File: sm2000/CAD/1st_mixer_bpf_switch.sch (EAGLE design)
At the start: 45 parts, among them U1 ADE-1, U2 PGA-103+

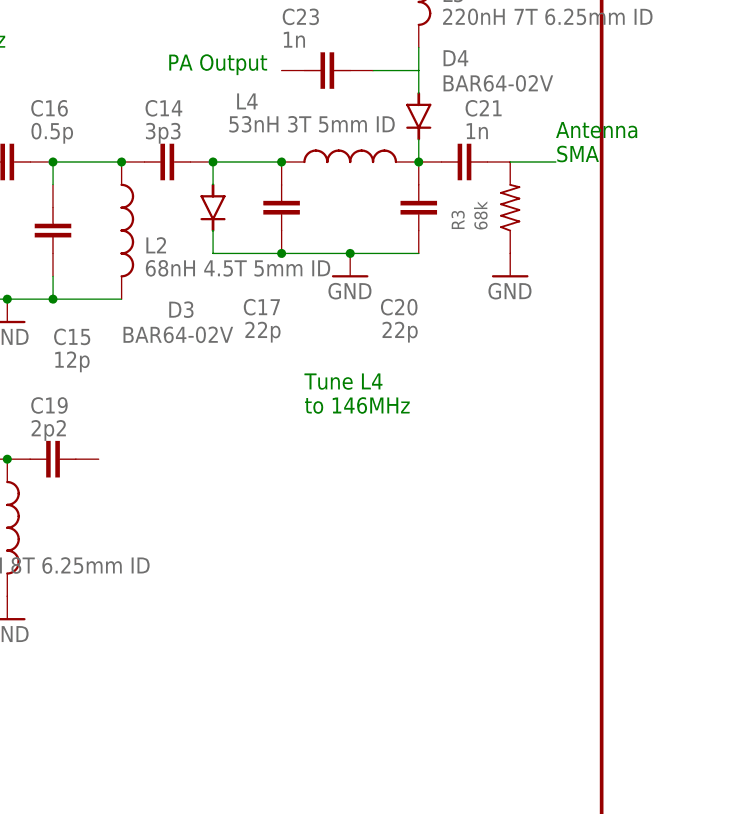
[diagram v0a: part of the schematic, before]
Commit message: added diode switch to TX 2nd lo and pwr sensor
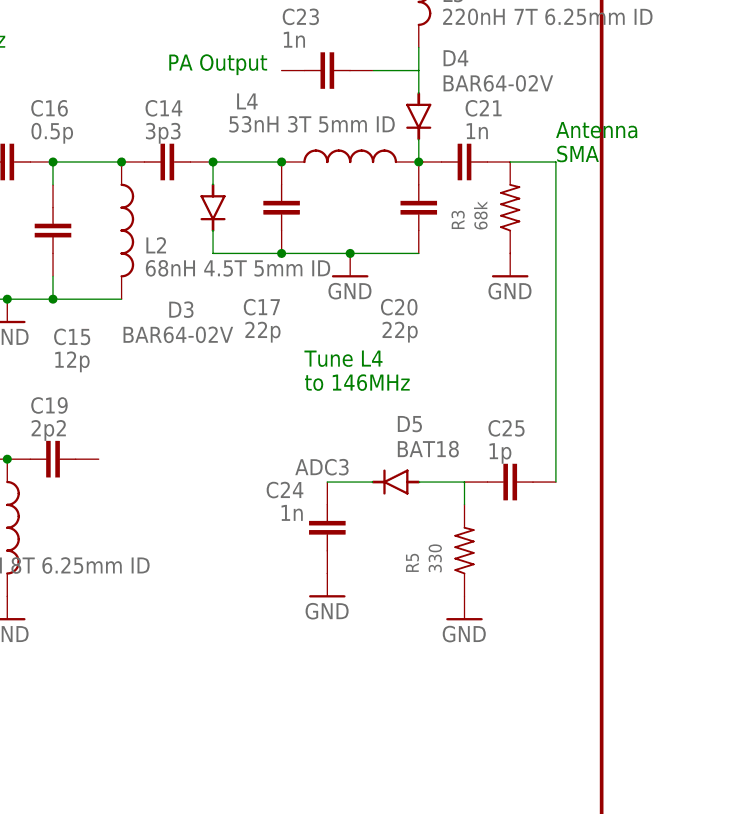
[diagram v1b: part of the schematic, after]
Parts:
- added C24: 1n, AA-ipc-7351-capacitor:CAPACITOR_0805
- added C25: 1p, AA-ipc-7351-capacitor:CAPACITOR_0805
- added D5: BAT18, _RoweTel:BAR64-02V
- added R5: 330, _RoweTel:RES0805
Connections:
- new net ADC3: C24.1, D5.C
- new net N$19: C25.2, D5.A, R5.2
- net GND: now also C24.2, R5.1
- net N$18: now also C25.1
